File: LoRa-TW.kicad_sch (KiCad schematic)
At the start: 48 parts, among them J1 MHF-I/U.FL, J2 Conn_02x06_2.0mm, J3 RFShield_OnePiece, U1 SX1262IMLTRT, X1 TCXO, 32MHz, 2.0x1.6mm

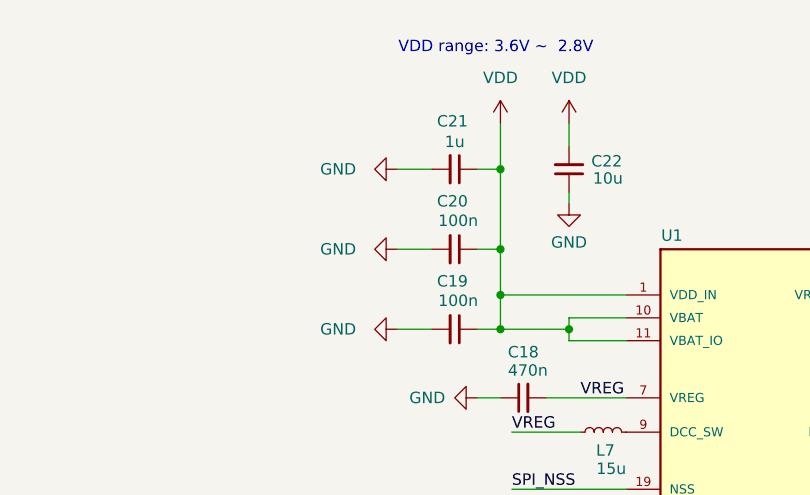
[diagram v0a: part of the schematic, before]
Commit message: update 15uH for sch and pcb
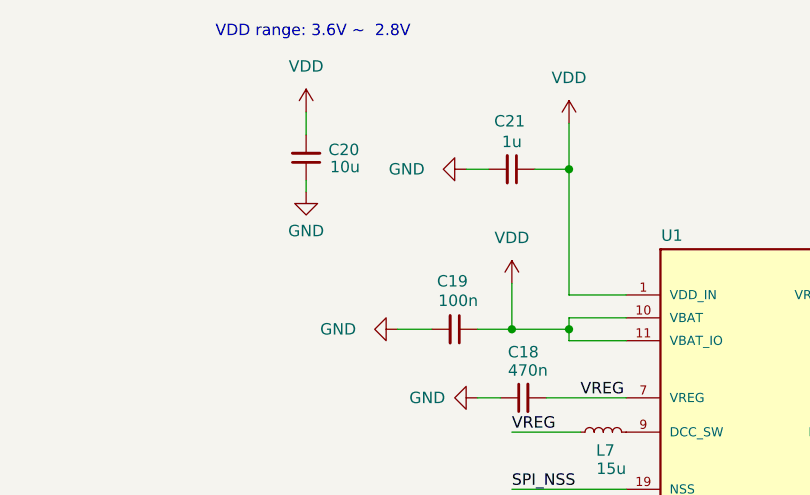
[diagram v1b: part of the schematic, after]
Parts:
- removed C20: 100n, LoRa-TW:C_HF_0402_1005Metric, symbol Device:C_Small
- C20: renamed from C22; Part No GRM21BR71A106MA3K -> GRM188Z71A106KA73D
- L7: footprint Inductor_SMD:L_0603_1608Metric -> Inductor_SMD:L_0805_2012Metric; Manufacturer Murata -> TDK; Part No LQW15AN9N1H00D -> MLZ2012M150WT000
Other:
- moved on the sheet: C20, C21

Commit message: prepare for BOM generation
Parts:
- C1, C19, C2, C20, C23, C4, C5, C6, C7, FB1, R1, R10, R4, R5, R6, R7, R8, R9: Manufacturer (none) -> Murata; Manufauturer Murata -> (none)
- C21: Manufacturer (none) -> Walsin; Manufauturer Walsin -> (none)
- FL1: Manufacturer (none) -> QUALCOMM/RF360; Manufauturer RF360 Europe GmbH - Qualcomm/TDK Joint -> (none)
- J1: Manufacturer (none) -> I-PEX; Manufauturer I-PEX -> (none)
- J2, J3: now not fitted
- S1: Manufacturer (none) -> PSemi; Manufauturer PSEMI -> (none)
- U1: Manufacturer (none) -> Semtech; Manufauturer Semtech -> (none); Part No (none) -> SX1262IMLTRT
- X1: Manufacturer (none) -> NDK; Part No (none) -> NT2016SA-32MHz-END4263A

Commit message: update description of components
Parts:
- C1: value 10P -> 10p
- C11: Part No GJM1555C1H1R8BB01D -> GJM1555C1H3R0BB01D
- C18: Part No GJM1555C1H3R3BB01D -> GRM155R71A474KE01D
- C20: Part No GRM188Z71A106KA73D -> GRM21BR71A106KA3L
- C5: Part No (none) -> GJM1555C1H2R4BB01D
- C6, C7: footprint Capacitor_SMD:C_0402_1005Metric -> LoRa-TW:C_HF_0402_1005Metric
- FB1: footprint Resistor_SMD:R_0402_1005Metric -> LoRa-TW:R_HF_0402_1005Metric
- L2: Manufacturer (none) -> Vishay; Part No (none) -> CRCW04020000Z0EDC
- R1: Manufacturer Murata -> Vishay
- R10, R4, R5, R6, R7, R8, R9: value 33 -> 22; Manufacturer Murata -> Vishay; Part No CRCW0402220RJNED -> CRCW040222R0JNED
- R2, R3: footprint Resistor_SMD:R_0402_1005Metric -> LoRa-TW:R_HF_0402_1005Metric; Manufacturer (none) -> Vishay; Part No (none) -> CRCW0402100RJNED
- X1: Part No NT2016SA-32MHz-END4263A -> NT2016SA-32MHz-END4263A/NT2016SF-END4263D-32M

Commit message: update SAW filter to use TST TA2710AA1322
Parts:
- FL1: footprint IC5_B39931B2645P810_QUA -> LoRa-TW:SAW_1411; Manufacturer QUALCOMM/RF360 -> TAI-SAW; Part No B39931B2645P810 -> TA2710AA1322
